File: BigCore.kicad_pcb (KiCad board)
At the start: 4 copper layers, 61 x 100 mm, 164 parts, among them J1 5V In, J10 Btn 3, J11 GND, J12 USB_C_Receptacle_USB2.0, J13 Line Out, J14 Servo 01, J15 Servo 02, J16 Servo 03, J17 Servo 04, J18 Servo 05, J19 Servo 06, J2 Vdrive In, J20 I2C, J21 RJ45, J22 WS2812, J23 5V Isolation, J24 GND Isolation, J3 JTAG, J4 DM3AT-SF-PEJM5, J5 Volume, J6 Btn 0, J7 RS485, J8 Btn 1, J9 Btn 2, Q1 SS8050-G, Q2 SS8050-G, SW1 Reset, SW2 Boot, SW3 Btn 0, SW4 Btn 1, SW5 Btn 2, SW6 Btn 3, U1 AP63203WU, U10 74LVC1G17, U2 AP2112K-3.3, U3 ESP32-WROOM-32E, U4 SN65HVD75DR, U5 USBLC6-2SC6, U6 CP2102N-Axx-xQFN24, U7 PCM5102A, U8 PCA9615DP, U9 74LVC1G17

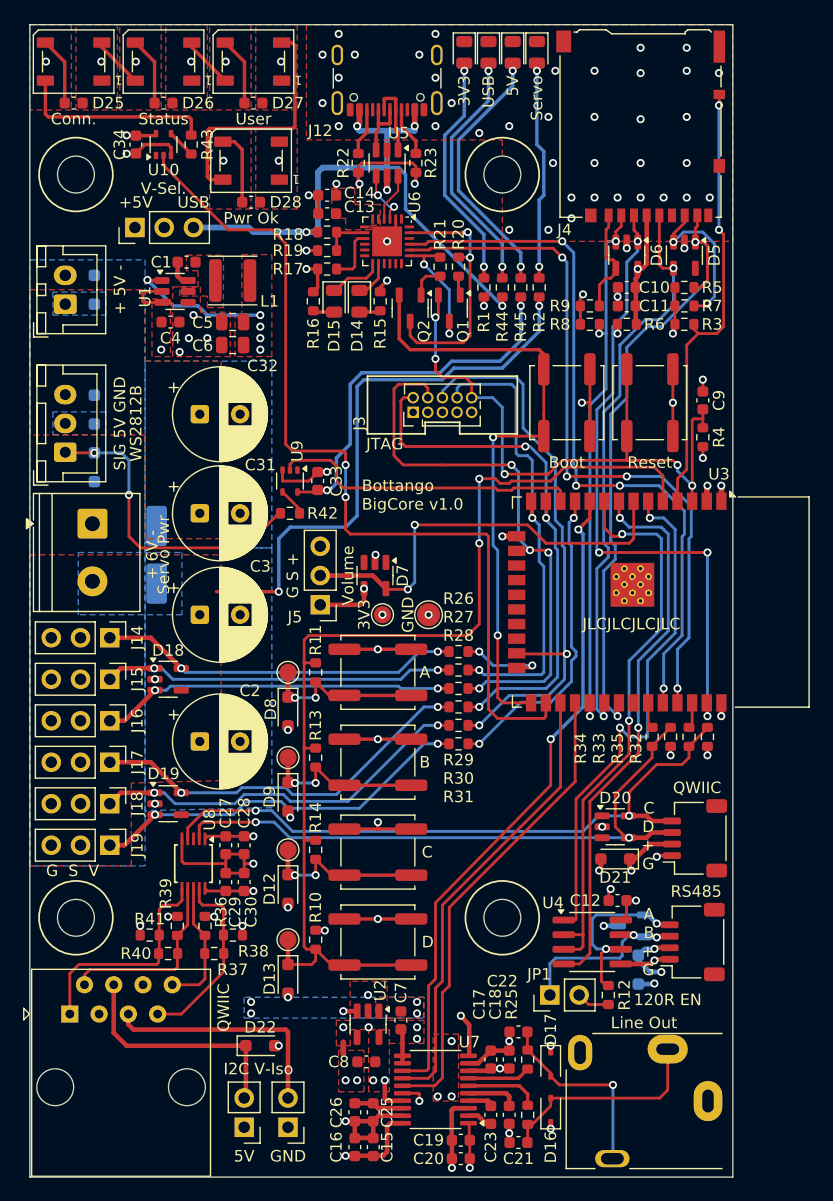
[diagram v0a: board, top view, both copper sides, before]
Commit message: - I2C entfernt - Logo hinzugefügt - Spannungsauswahl für Audio (USB oder +5V) hinzugefügt - Spannung für WS2812 LEDs ändert sich jetzt zusammen mit +5VD Auswahl
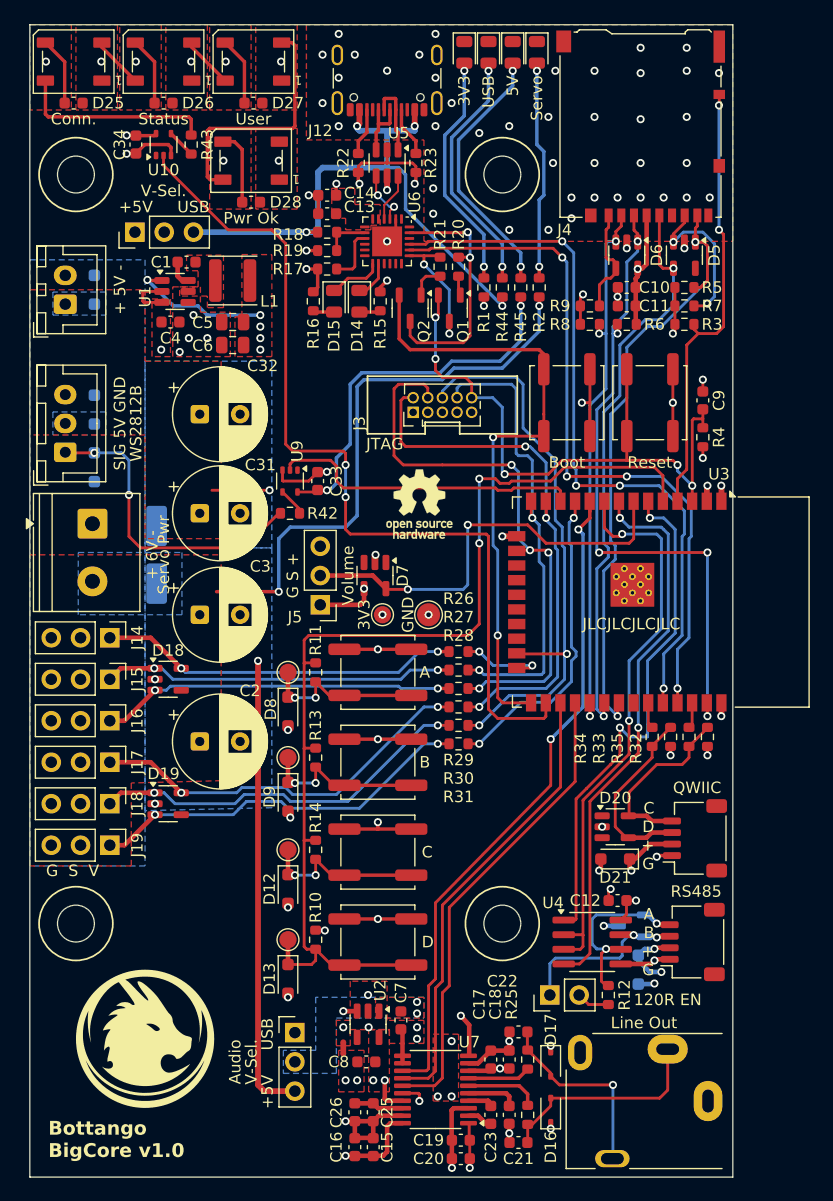
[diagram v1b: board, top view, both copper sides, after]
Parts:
- removed C27, C29: 100n, Capacitor_SMD:C_0603_1608Metric
- removed C28, C30: 1µ, Capacitor_SMD:C_0603_1608Metric
- removed D22: TSD05DYFR, Diode_SMD:D_SOD-323_HandSoldering
- removed J21: RJ45, Connector_RJ:RJ45_Amphenol_54602-x08_Horizontal
- removed J23: 5V Isolation, Connector_PinHeader_2.54mm:PinHeader_1x02_P2.54mm_Vertical
- removed J24: GND Isolation, Connector_PinHeader_2.54mm:PinHeader_1x02_P2.54mm_Vertical
- removed R36, R38, R39, R41: 390, Resistor_SMD:R_0603_1608Metric
- removed R37, R40: 100, Resistor_SMD:R_0603_1608Metric
- removed U8: PCA9615DP, Package_SO:TSSOP-10_3x3mm_P0.5mm
- added G***: LOGO, Avatar:Avatar_12x12, F.Cu at (93.0, 190.0)
- added JP3: 5V Selection Analog, Connector_PinHeader_2.54mm:PinHeader_1x03_P2.54mm_Vertical, F.Cu at (106.0, 189.5)
- added REF**: OSHW-Logo_5.7x6mm_SilkScreen, Symbol:OSHW-Logo_5.7x6mm_SilkScreen, F.Cu at (116.8, 143.6)
- JP2: value 5V Selection -> 5V Selection Digital
- moved H3 0.50 mm to (87.0, 180.0)
- moved H4 0.50 mm to (124.0, 180.0)
- moved JP2 0.40 mm to (92.1, 120.0)
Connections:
- C34 pad 1: +5V -> +5VD
- C35 pad 1: +5V -> +5VD
- C36 pad 1: +5V -> +5VD
- C37 pad 1: +5V -> +5VD
- C38 pad 1: +5V -> +5VD
- C4 pad 1: /Power Supply/5V_In -> +5VD
- C7 pad 1: +5V -> /Power Supply/5VA_In
- D25 pad 1: +5V -> +5VD
- D26 pad 1: +5V -> +5VD
- D27 pad 1: +5V -> +5VD
- D28 pad 1: +5V -> +5VD
- JP2 pad 2: /Power Supply/5V_In -> +5VD
- U1 pad 2: /Power Supply/5V_In -> +5VD
- U1 pad 3: /Power Supply/5V_In -> +5VD
- U10 pad 5: +5V -> +5VD
- U2 pad 1: +5V -> /Power Supply/5VA_In
- U2 pad 3: +5V -> /Power Supply/5VA_In
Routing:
- net VBUS: track 55.5 -> 140.7 mm, vias 5 -> 6
- net +5V: track 52.6 -> 95.4 mm, vias 15 -> 3
- net Net-(J20-Pin_4): track 56.9 -> 15.7 mm, vias 2 -> 0
- net Net-(J20-Pin_3): track 55.3 -> 16.1 mm, vias 2 -> 0
- net Net-(J23-Pin_2): track 20.8 -> 0.00 mm
- net Net-(D22-K): track 20.7 -> 0.00 mm
- net Net-(U8-DSCLM): track 19.5 -> 0.00 mm
- net +5VD: track 0.00 -> 17.1 mm, vias 0 -> 6
- net Net-(U8-DSCLP): track 16.4 -> 0.00 mm
- net Net-(U8-DSDAM): track 16.3 -> 0.00 mm
- net GND: track 141.4 -> 125.6 mm, vias 93 -> 92
- net /Power Supply/5V_In: track 14.9 -> 0.00 mm, vias 1 -> 0
- net Net-(U8-DSDAP): track 11.3 -> 0.00 mm
- net +3.3V: track 70.9 -> 66.2 mm, vias 25 -> 24
- net /Power Supply/5VA_In: track 0.00 -> 1.20 mm, vias 0 -> 3
- added copper zone on F.Cu, net +5VD
- added copper zone on In2.Cu, net +5VD
- added copper zone on B.Cu, net /Power Supply/5VA_In
- added copper zone on F.Cu, net /Power Supply/5VA_In
- removed copper zone on F.Cu, net /Power Supply/5V_In
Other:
- board text added: "Audio"
- board text removed: "I2C V-Iso"

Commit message: Changed the WS2812 driver IC Optimized the Analog GND and AVCC routing Changed RS485 driver Removed TVS Diode at the RS485 driver (already has 15kV rating)
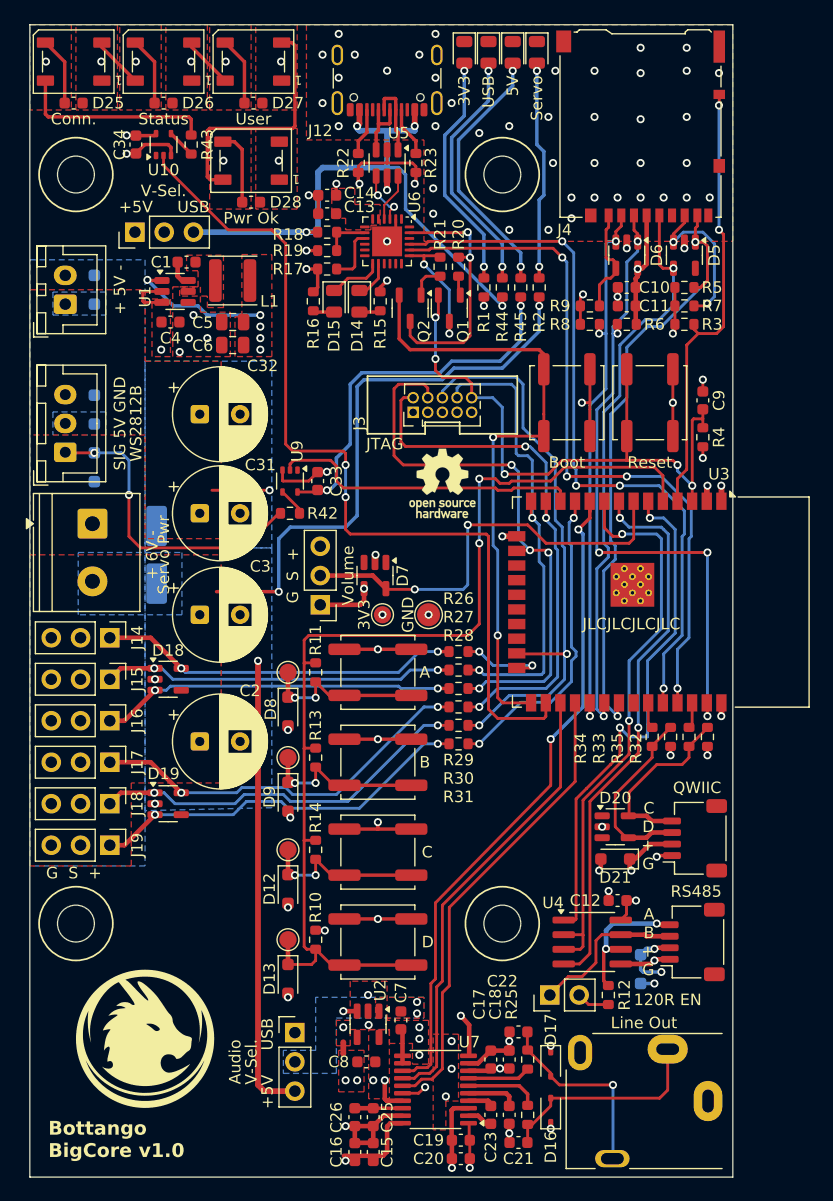
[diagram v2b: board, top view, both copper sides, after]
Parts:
- removed D11: ESDS552, Package_TO_SOT_SMD:SOT-23-3
- removed REF**: OSHW-Logo_5.7x6mm_SilkScreen, Symbol:OSHW-Logo_5.7x6mm_SilkScreen
- added H5: Logo_Open_Hardware_Small, Symbol:OSHW-Logo_5.7x6mm_SilkScreen, F.Cu at (118.8, 141.8)
- U10, U9: value 74LVC1G17 -> 74AHCT1G17
- U4: value SN65HVD75DR -> ST3485EBDR
- moved C25 0.43 mm to (112.8, 196.8)
- moved C26 0.43 mm to (111.2, 196.8)
- moved C15 0.42 mm to (112.8, 199.8)
- moved C16 0.42 mm to (111.2, 199.8)
- moved D10 0.21 mm to (136.0, 183.9)
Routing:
- net /Controller/RS485_A: track 15.8 -> 12.1 mm
- net /Controller/RS485_B: track 16.1 -> 13.8 mm, vias 2 -> 0
- net GND: track 125.6 -> 124.1 mm
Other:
- board text removed: "G S V"

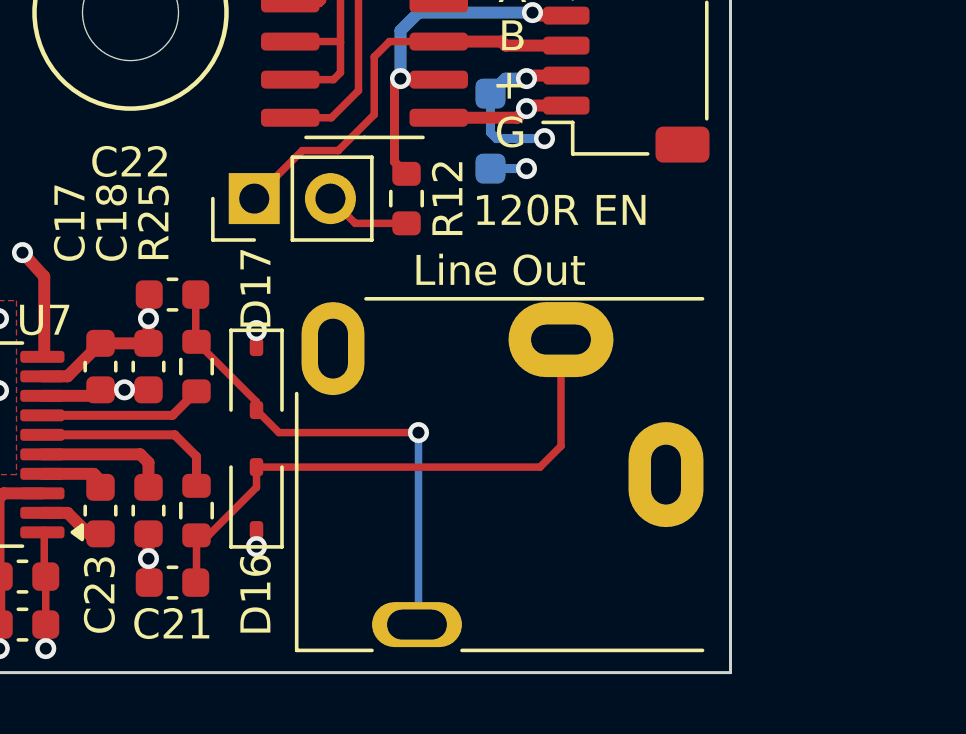
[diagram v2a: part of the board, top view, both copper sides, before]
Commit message: Changed Line Out Connector
Changed Line Out Connector
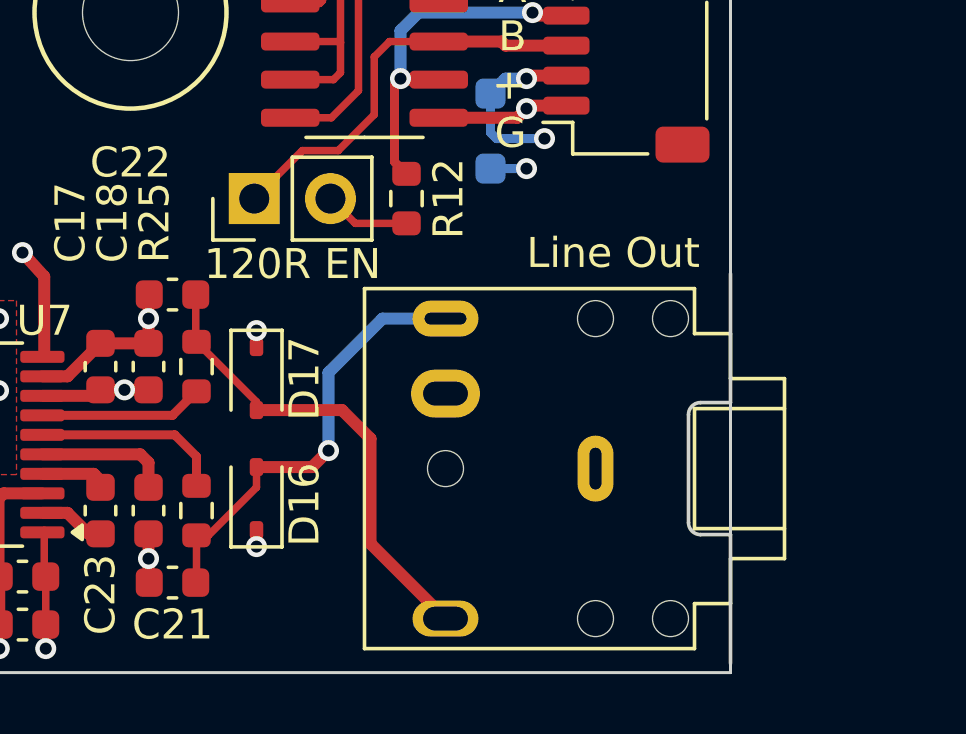
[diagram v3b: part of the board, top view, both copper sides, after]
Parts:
- J13: footprint Connector_Audio:Jack_3.5mm_CUI_SJ1-3514N_Horizontal -> Connector_Audio:Jack_3.5mm_CUI_SJ1-3524N_Horizontal
- moved J13 2.36 mm to (139.5, 195.2), turned to 90 degrees
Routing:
- net Net-(D16-A2): track 18.9 -> 14.8 mm, vias 0 -> 1
- net Net-(D17-A2): track 16.9 -> 16.1 mm, vias 1 -> 0

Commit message: Footprint changes
Changed WS2812 from 5050 to 2020
Changed ESP32 to correct revision
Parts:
- D25, D26, D27, D28: footprint LED_SMD:LED_WS2812B_PLCC4_5.0x5.0mm_P3.2mm -> LED_SMD:LED_WS2812B-2020_PLCC4_2.0x2.0mm
- U3: footprint RF_Module:ESP32-WROOM-32D -> RF_Module:ESP32-WROOM-32E
- moved C38 10.0 mm to (104.4, 107.6)
- moved D28 8.88 mm to (104.4, 105.2)
- moved C37 4.18 mm to (98.4, 107.6)
- moved D27 4.00 mm to (98.4, 105.2)
- moved U3 3.04 mm to (137.8, 152.1)
- moved C36 2.51 mm to (92.4, 107.6)
- moved D26 2.20 mm to (92.4, 105.2)
- moved C35 1.26 mm to (86.4, 107.6)
- moved D25 0.40 mm to (86.4, 105.2)
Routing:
- net Net-(D27-DOUT): track 21.5 -> 4.63 mm
- net GND: track 124.1 -> 115.5 mm
- net Net-(D25-DIN): track 17.1 -> 18.7 mm
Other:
- outline, holes or cut-outs redrawn
- board text added: "Link"
- board text removed: "Conn."

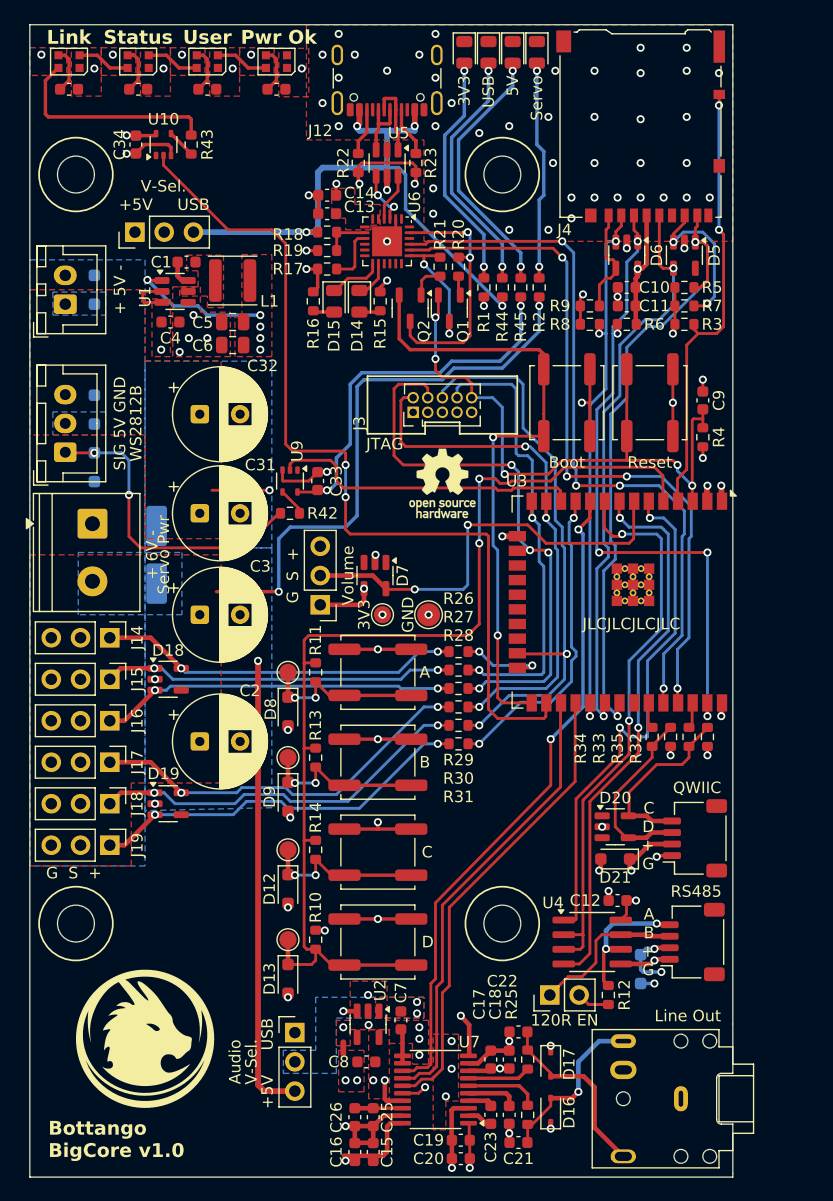
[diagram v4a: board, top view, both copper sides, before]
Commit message: First Manufactured Version
A few silkscreen changes
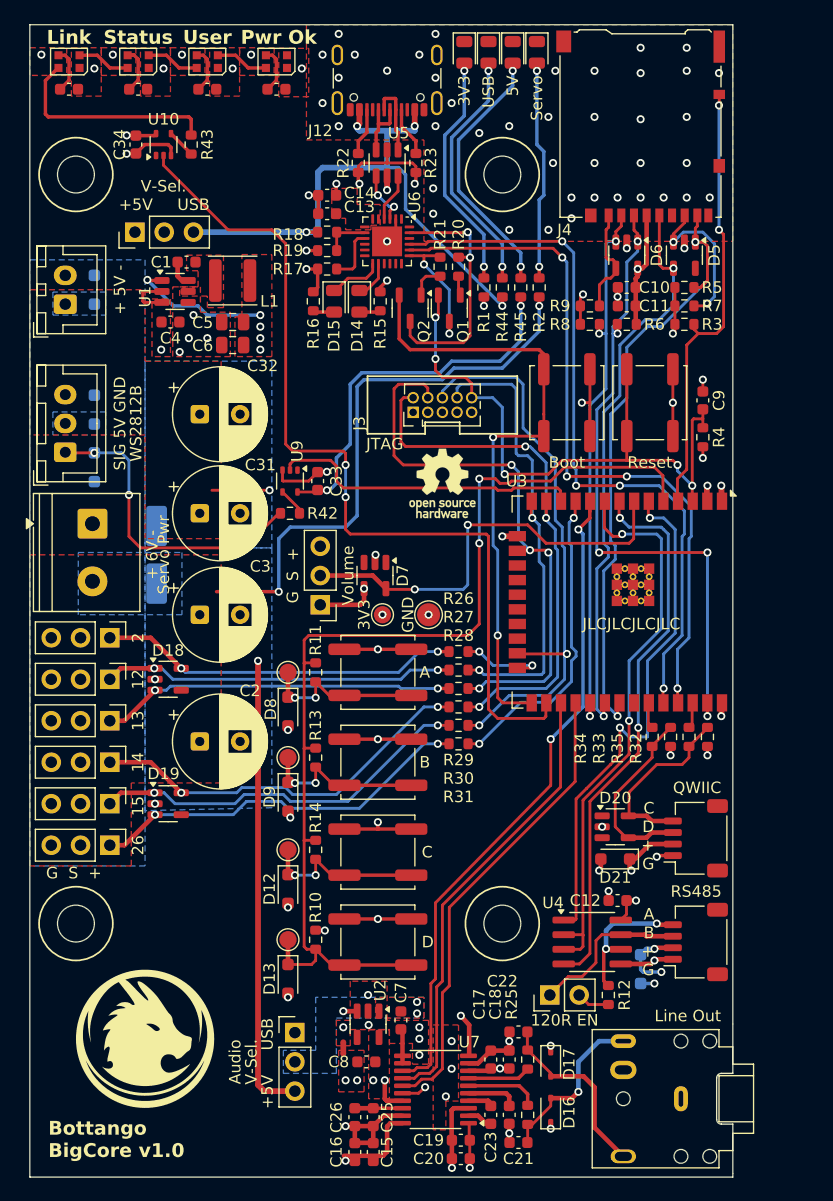
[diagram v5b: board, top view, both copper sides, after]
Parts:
- moved J7 0.28 mm to (140.8, 181.6)
- moved J20 0.08 mm to (140.8, 172.6)
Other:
- board text added: "12"
- board text added: "13"
- board text added: "14"
- board text added: "15"
- board text added: "2"
- board text added: "26"

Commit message: SD-Card Fix
- DAT0 and DAT1 where flipped
- Changed footprint for ESD-Diodes D16 and D17 to be more hand-soldering friendly
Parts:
- D16, D17: footprint Diode_SMD:D_SOD-323 -> Diode_SMD:D_SOD-323_HandSoldering
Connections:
- D5 pad 1: /Controller/SD_DAT0 -> Net-(J4-DAT1)
- D5 pad 3: Net-(J4-DAT0) -> /Controller/SD_DAT0
- J4 pad 7: Net-(J4-DAT0) -> /Controller/SD_DAT0
- J4 pad 8: /Controller/SD_DAT0 -> Net-(J4-DAT1)
- R5 pad 2: /Controller/SD_DAT0 -> Net-(J4-DAT1)
- R7 pad 2: Net-(J4-DAT0) -> /Controller/SD_DAT0
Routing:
- net Net-(J4-DAT0): track 13.7 -> 0.00 mm, vias 2 -> 0
- net Net-(J4-DAT1): track 0.00 -> 8.00 mm
- net /Controller/SD_DAT0: track 56.5 -> 52.7 mm, vias 2 -> 3
- net /Controller/SD_Detect: track 39.0 -> 37.5 mm
- net GNDA: track 15.3 -> 16.1 mm

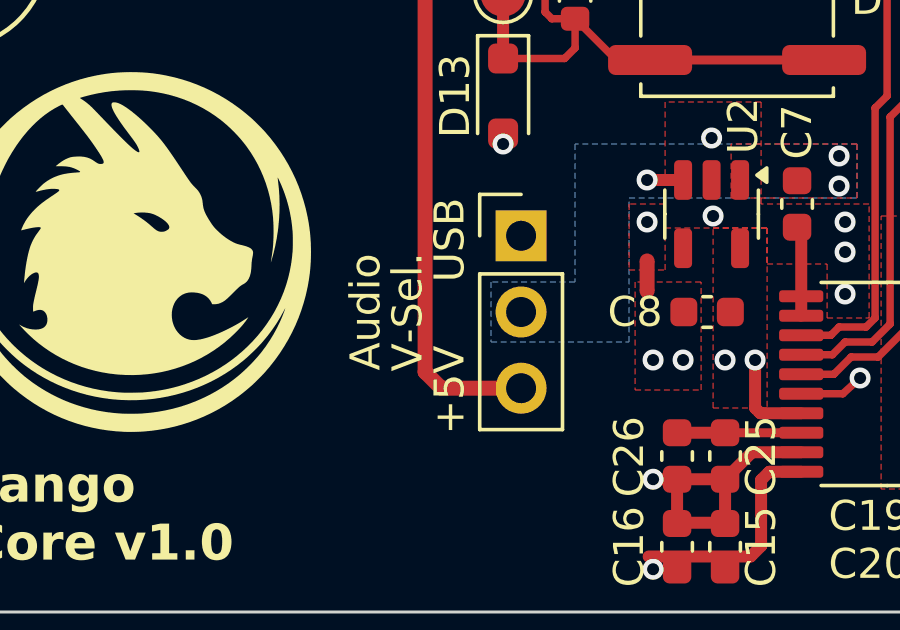
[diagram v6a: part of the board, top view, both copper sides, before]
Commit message: Silkscreen fix
Fixed wrong silkcreen text for the DAC Voltage-Source. USB and +5V are flipped
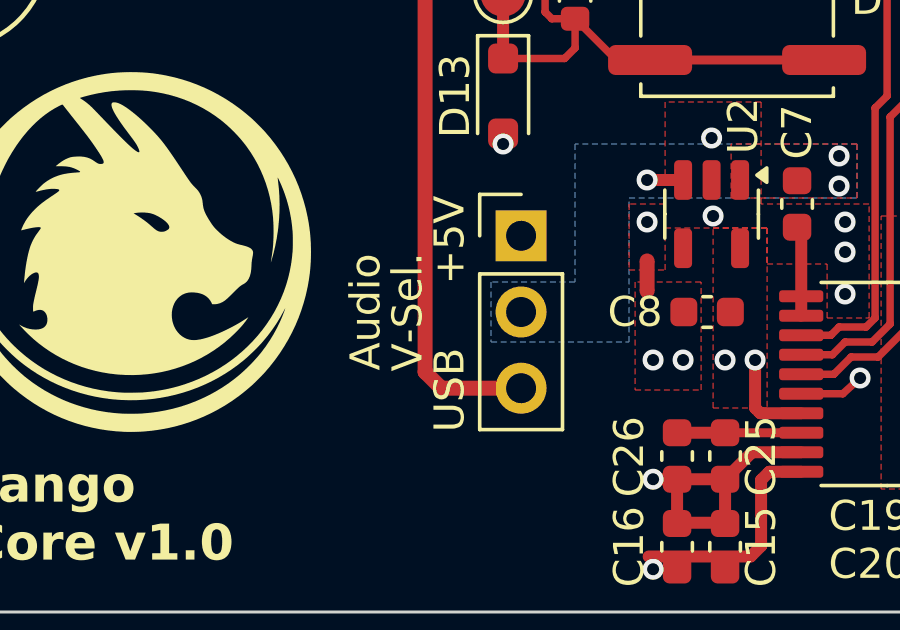
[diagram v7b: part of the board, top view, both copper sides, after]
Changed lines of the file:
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@@
 	)
 	(gr_text "+5V"
-		(at 104.2 194.6 90)
+		(at 104.2 189.6 90)
 		(layer "F.SilkS")
 		(effects
@@
 	)
 	(gr_text "USB"
-		(at 104.2 189.6 90)
+		(at 104.2 194.6 90)
 		(layer "F.SilkS")
 		(effects
